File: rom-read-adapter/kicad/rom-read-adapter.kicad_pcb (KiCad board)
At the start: 2 copper layers, 100 x 100 mm, 27 parts

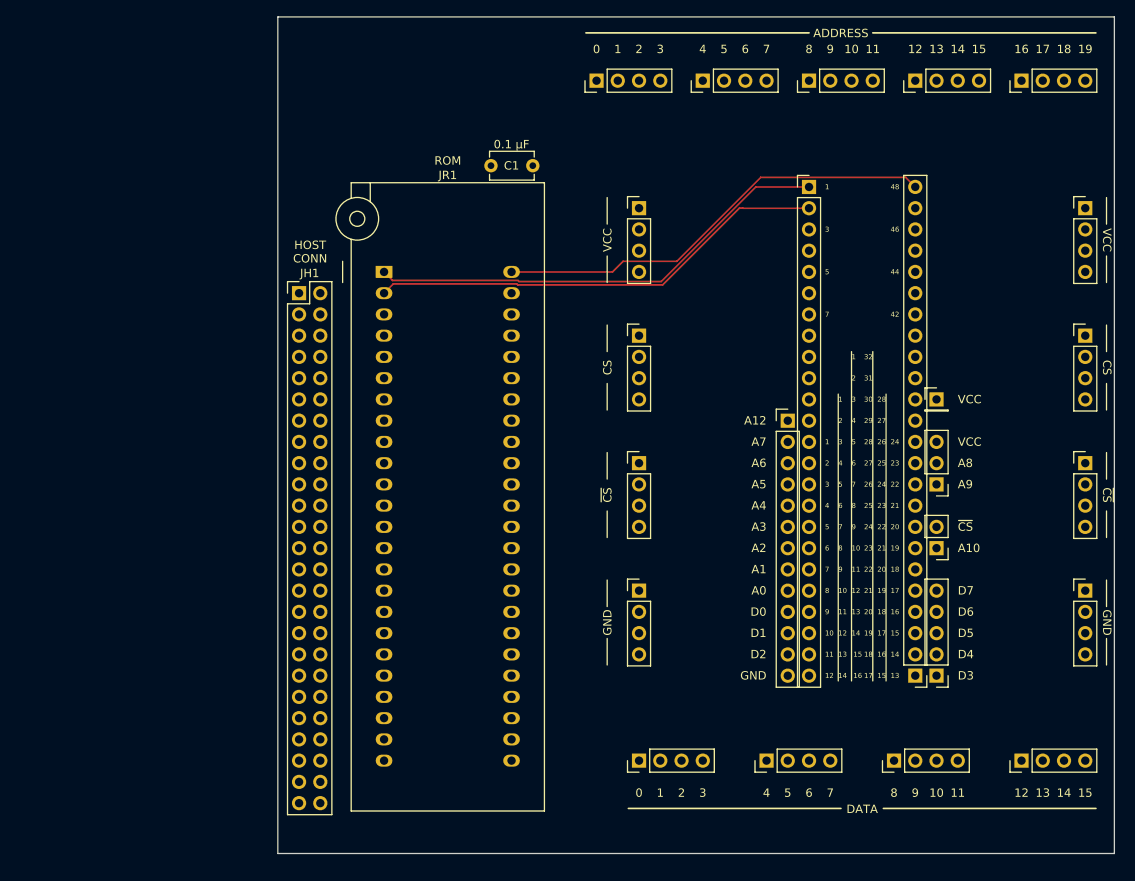
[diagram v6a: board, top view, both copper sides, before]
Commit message: WIP rom-reader-adapter pcb: Move Host Conn
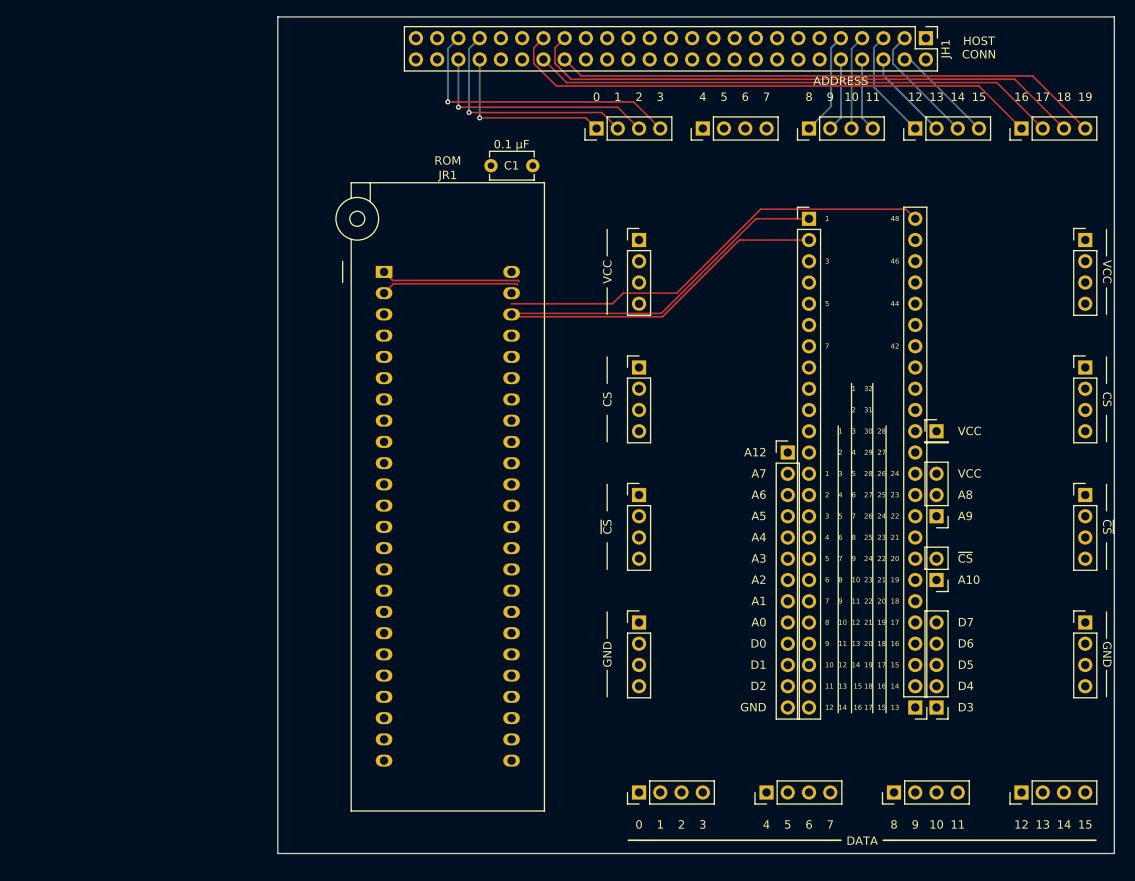
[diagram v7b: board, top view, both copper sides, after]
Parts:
- moved JH1 80.9 mm to (179.1, 53.3), turned to -90 degrees
- moved JH11 5.72 mm to (139.7, 64.1)
- moved JH12 5.72 mm to (152.4, 64.1)
- moved JH13 5.72 mm to (165.1, 64.1)
- moved JH14 5.72 mm to (177.8, 64.1)
- moved JH15 5.72 mm to (190.5, 64.1)
- moved JH2 3.81 mm to (162.6, 102.9)
- moved JH21 3.81 mm to (144.8, 143.5)
- moved JH22 3.81 mm to (160.0, 143.5)
- moved JH23 3.81 mm to (175.3, 143.5)
- moved JH24 3.81 mm to (190.5, 143.5)
- moved JH3 3.81 mm to (180.3, 133.3)
- moved JH31 3.81 mm to (144.8, 77.5)
- moved JH34 3.81 mm to (144.8, 123.2)
- moved JH4 3.81 mm to (180.3, 118.1)
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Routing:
- net A18: track 0.00 -> 67.6 mm
- net A19: track 0.00 -> 65.6 mm
- net A16: track 0.00 -> 65.0 mm
- net A17: track 0.00 -> 63.1 mm
- net A3: track 0.00 -> 34.9 mm, vias 0 -> 1
- net A2: track 0.00 -> 28.4 mm, vias 0 -> 1
- net A1: track 0.00 -> 28.0 mm, vias 0 -> 1
- net A0: track 0.00 -> 21.5 mm, vias 0 -> 1
- net A14: track 0.00 -> 14.6 mm
- net A12: track 0.00 -> 13.3 mm
- net A8: track 0.00 -> 12.4 mm
- net A15: track 0.00 -> 12.3 mm
- net A10: track 0.00 -> 11.3 mm
- net A13: track 0.00 -> 10.9 mm
- net A9: track 0.00 -> 8.78 mm
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
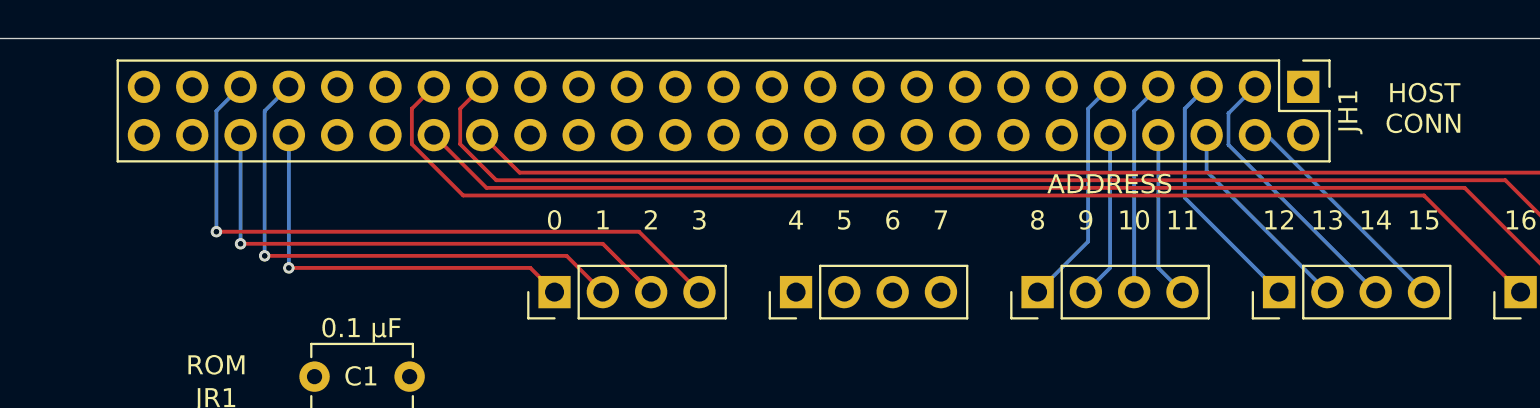
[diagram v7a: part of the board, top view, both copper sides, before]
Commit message: WIP rom-read-adapter pcb: Finish routing address pins
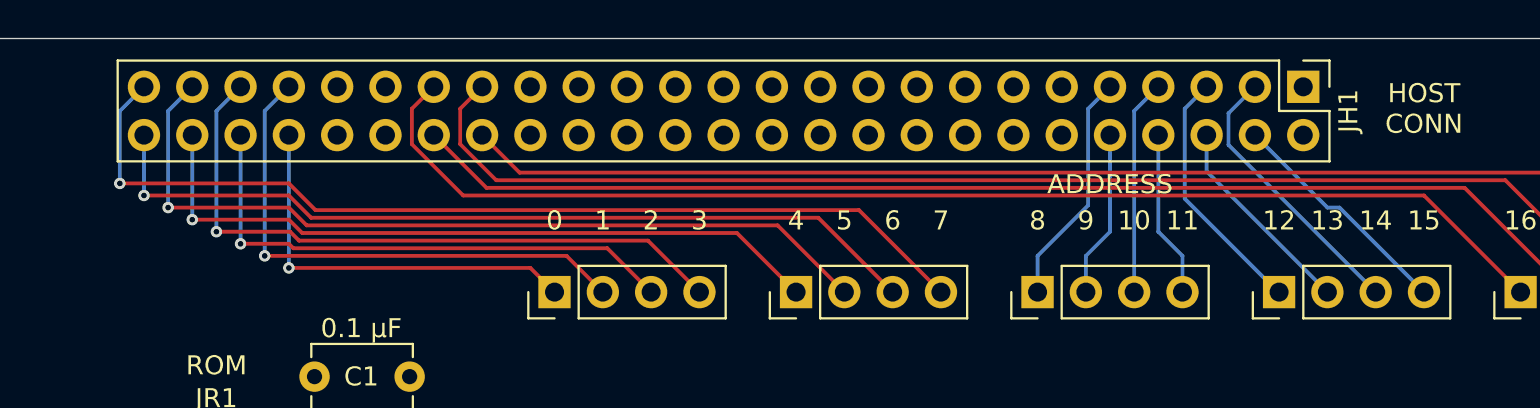
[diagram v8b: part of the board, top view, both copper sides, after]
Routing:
- net A7: track 0.00 -> 51.2 mm, vias 0 -> 1
- net A6: track 0.00 -> 44.6 mm, vias 0 -> 1
- net A5: track 0.00 -> 44.3 mm, vias 0 -> 1
- net A4: track 0.00 -> 37.8 mm, vias 0 -> 1
